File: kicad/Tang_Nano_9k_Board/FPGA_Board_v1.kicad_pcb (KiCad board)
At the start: 2 copper layers, 11 parts, among them U3 TBD62083AFG, U5 TBD62783A

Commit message: making pcb board
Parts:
- added H1: MountingHole, MountingHole:MountingHole_2.1mm, F.Cu at (103.5, 56.5)
- added H2: MountingHole, MountingHole:MountingHole_2.1mm, F.Cu at (192.4, 56.5)
- added H3: MountingHole, MountingHole:MountingHole_2.1mm, F.Cu at (192.4, 147.3)
- added H4: MountingHole, MountingHole:MountingHole_2.1mm, F.Cu at (103.5, 147.3)
- added J1: Conn_01x24, Connector_PinHeader_2.54mm:PinHeader_1x24_P2.54mm_Vertical, F.Cu at (101.6, 71.1)
- added J2: Conn_01x24, Connector_PinHeader_2.54mm:PinHeader_1x24_P2.54mm_Vertical, F.Cu at (133.3, 71.1)
- added J3: Conn_01x08, Connector_PinHeader_2.54mm:PinHeader_1x08_P2.54mm_Vertical, F.Cu at (192.4, 120.7)
- added J4: Conn_01x04, Connector_PinHeader_2.54mm:PinHeader_1x04_P2.54mm_Vertical, F.Cu at (113.7, 140.3)
- added J5: Conn_01x04, Connector_PinHeader_2.54mm:PinHeader_1x04_P2.54mm_Vertical, F.Cu at (120.2, 140.3)
- added J6: Conn_01x04, Connector_PinHeader_2.54mm:PinHeader_1x04_P2.54mm_Vertical, F.Cu at (127.0, 140.3)
- added J7: Conn_01x04, Connector_PinHeader_2.54mm:PinHeader_1x04_P2.54mm_Vertical, F.Cu at (133.3, 140.3)
- added SW1: SW_DIP_x08, Button_Switch_THT:SW_DIP_SPSTx08_Slide_9.78x22.5mm_W7.62mm_P2.54mm, F.Cu at (162.6, 139.7)
- added SW2: SW_Push, Button_Switch_SMD:Panasonic_EVQPUJ_EVQPUA, F.Cu at (180.3, 130.8)
- added SW3: SW_Push, Button_Switch_SMD:Panasonic_EVQPUJ_EVQPUA, F.Cu at (180.3, 137.4)
- added SW4: SW_Push, Button_Switch_SMD:Panasonic_EVQPUJ_EVQPUA, F.Cu at (180.3, 143.9)
- added U2: ~, BFP_footprints:OSL641501-BX, F.Cu at (177.2, 82.5)
- added U4: 74HC138, Package_DIP:CERDIP-16_W7.62mm_SideBrazed, F.Cu at (142.9, 107.3)
- R18, R19, R20, R21, R22, R23, R24, R25: value 600 -> 750; moved to B.Cu
- U1: footprint BFP:Tang_Nano_9K -> BFP_footprints:Tang_Nano_9K
- moved R22 81.4 mm to (187.3, 92.7), turned to 180 degrees
- moved R21 80.6 mm to (187.3, 86.4), turned to 180 degrees
- moved R18 80.4 mm to (187.3, 73.7), turned to 180 degrees
- moved R23 76.4 mm to (187.3, 80.0), turned to 180 degrees
- moved R19 75.3 mm to (173.4, 92.7), turned to 180 degrees
- moved R20 69.7 mm to (173.4, 86.4), turned to 180 degrees
- moved R24 61.9 mm to (173.4, 80.0), turned to 180 degrees
- moved R25 60.8 mm to (173.4, 73.7), turned to 180 degrees
- moved U5 47.2 mm to (159.4, 107.3)
- moved U1 42.5 mm to (117.5, 103.6)
- moved U3 38.8 mm to (142.9, 78.8)
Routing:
- net Net-(J2-Pin_14): track 0.00 -> 127.9 mm
- net Net-(J1-Pin_1): track 0.00 -> 125.2 mm
- net Net-(J2-Pin_13): track 0.00 -> 124.8 mm
- net Net-(J2-Pin_12): track 0.00 -> 123.6 mm
- net Net-(J1-Pin_2): track 0.00 -> 120.5 mm
- net Net-(J1-Pin_3): track 0.00 -> 116.0 mm
- net /C8: track 0.00 -> 112.2 mm
- net /C7: track 0.00 -> 109.2 mm
- net /C6: track 0.00 -> 106.1 mm
- net /C5: track 0.00 -> 103.0 mm
- net /C4: track 0.00 -> 100.0 mm
- net Net-(J2-Pin_2): track 0.00 -> 97.5 mm
- net /C3: track 0.00 -> 96.9 mm
- net /C2: track 0.00 -> 93.8 mm
- net Net-(J2-Pin_3): track 0.00 -> 92.8 mm
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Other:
- board outline added: 100 x 100 mm

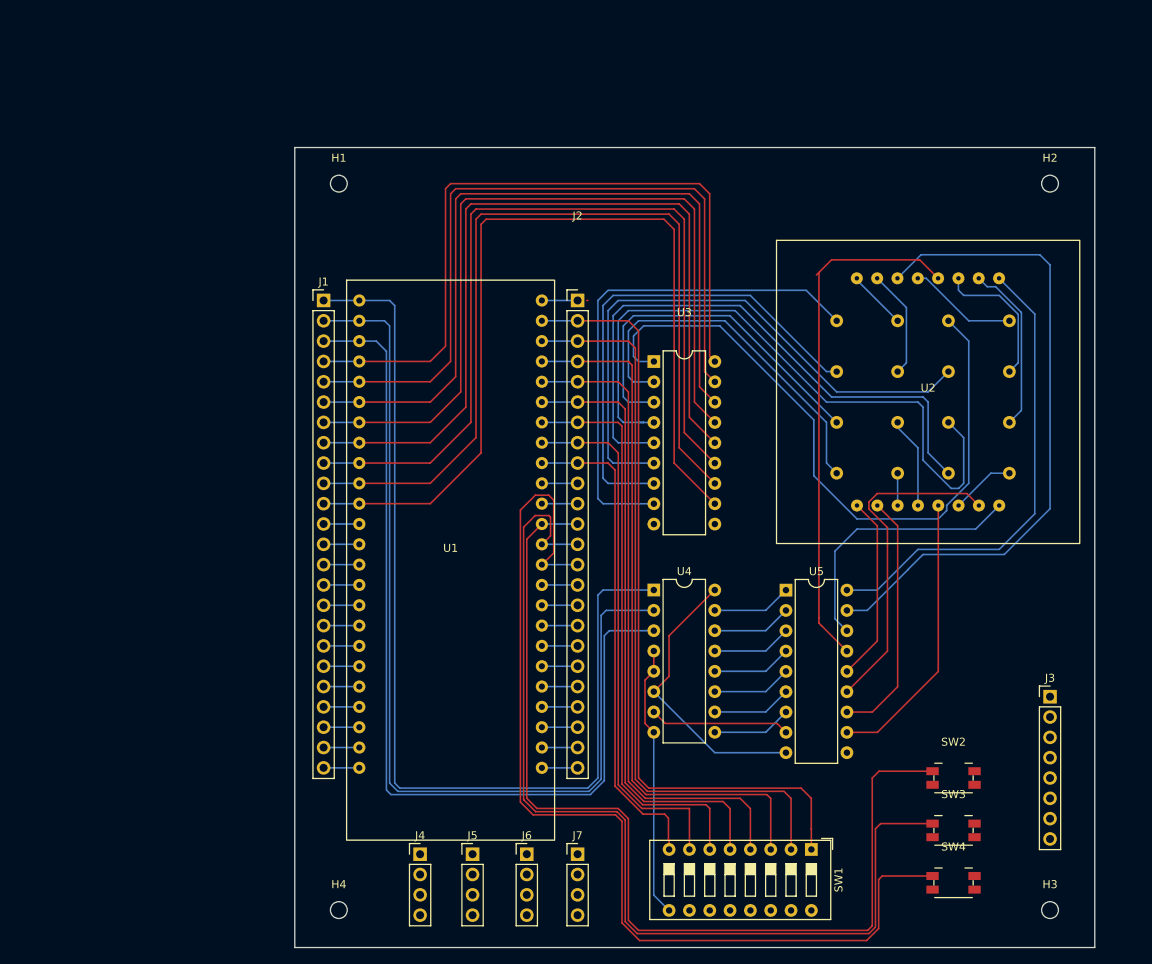
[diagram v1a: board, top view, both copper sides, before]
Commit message: set pcb position
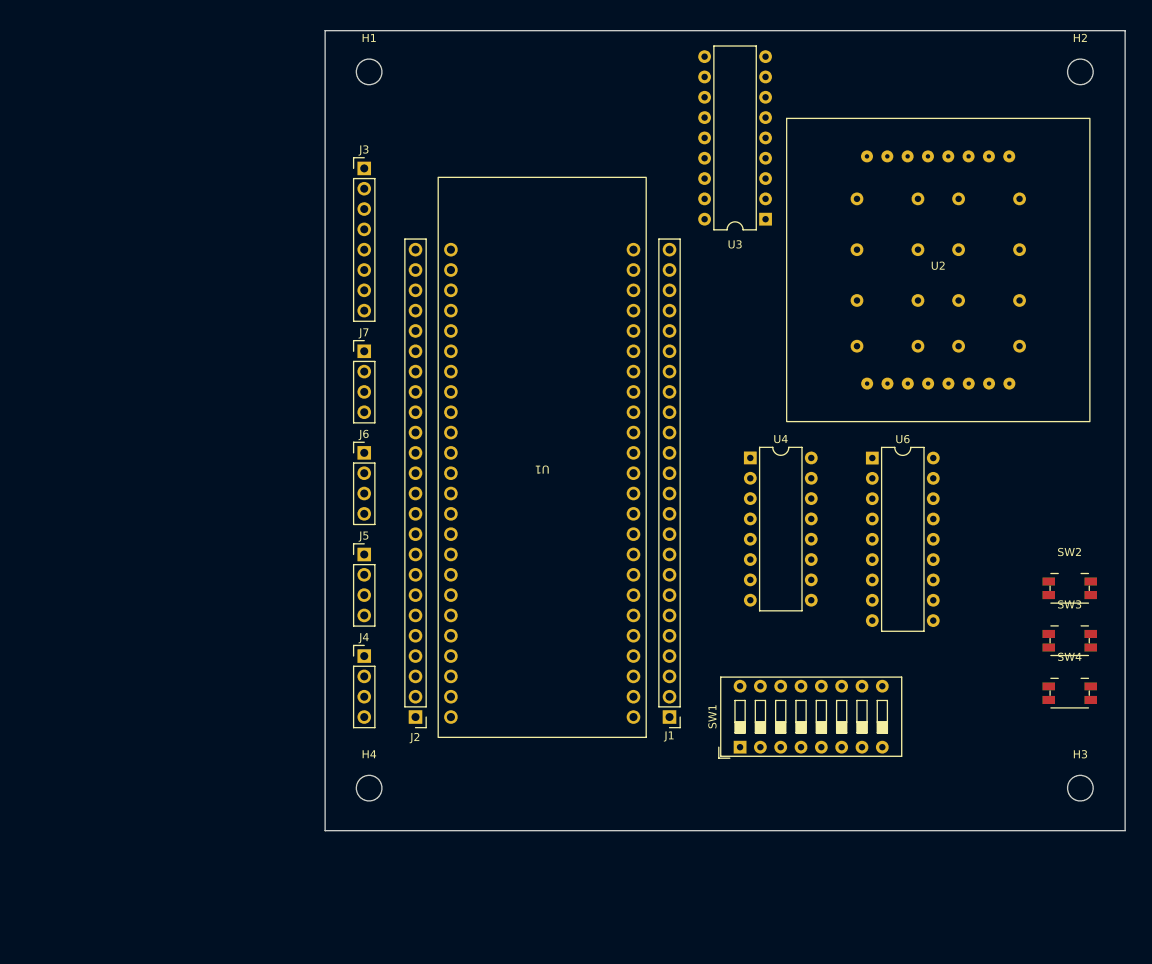
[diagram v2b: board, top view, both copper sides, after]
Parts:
- removed U5: TBD62783A, Package_DIP:DIP-18_W7.62mm
- added U6: TBD62786APG, Package_DIP:DIP-18_W7.62mm, F.Cu at (170.2, 90.8)
- H1, H2, H3, H4: footprint MountingHole:MountingHole_2.1mm -> MountingHole:MountingHole_3.2mm_M3
- moved J3 108.2 mm to (106.7, 54.6)
- moved J7 68.3 mm to (106.7, 77.5)
- moved J1 67.7 mm to (144.8, 123.2), turned to 180 degrees
- moved J2 55.9 mm to (113.1, 123.2), turned to 180 degrees
- moved J6 54.1 mm to (106.7, 90.2)
- moved J5 39.8 mm to (106.7, 102.9)
- moved SW2 27.8 mm to (194.9, 107.1)
- moved SW3 27.8 mm to (194.9, 113.7)
- moved SW4 27.8 mm to (194.9, 120.2)
- moved J4 25.7 mm to (106.7, 115.6)
- moved U3 22.6 mm to (156.8, 61.0), turned to 180 degrees
- moved U4 20.4 mm to (154.9, 90.8)
- moved U1 17.2 mm to (128.9, 90.7), turned to 180 degrees
- moved R19 16.1 mm to (175.9, 76.8)
- moved R22 15.9 mm to (188.6, 76.8)
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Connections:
- net Net-(J1-Pin_2) renamed /A1
- J1 pad 1: Net-(J1-Pin_1) -> /A2
- J1 pad 3: Net-(J1-Pin_3) -> /A0
- U1 pad 1: Net-(J1-Pin_1) -> /A2
- U1 pad 3: Net-(J1-Pin_3) -> /A0
- U4 pad 1: Net-(J1-Pin_1) -> /A0
- U4 pad 3: Net-(J1-Pin_3) -> /A2
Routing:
- net Net-(J2-Pin_14): track 127.9 -> 0.00 mm
- net Net-(J1-Pin_1): track 125.2 -> 0.00 mm
- net Net-(J2-Pin_13): track 124.8 -> 0.00 mm
- net Net-(J2-Pin_12): track 123.6 -> 0.00 mm
- net /A1: track 120.5 -> 0.00 mm
- net Net-(J1-Pin_3): track 116.0 -> 0.00 mm
- net /C8: track 112.2 -> 0.00 mm
- net /C7: track 109.2 -> 0.00 mm
- net /C6: track 106.1 -> 0.00 mm
- net /C5: track 103.0 -> 0.00 mm
- net /C4: track 100.0 -> 0.00 mm
- net Net-(J2-Pin_2): track 97.5 -> 0.00 mm
- net /C3: track 96.9 -> 0.00 mm
- net /C2: track 93.8 -> 0.00 mm
- net Net-(J2-Pin_3): track 92.8 -> 0.00 mm
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
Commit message: finish schematic, design PCB board
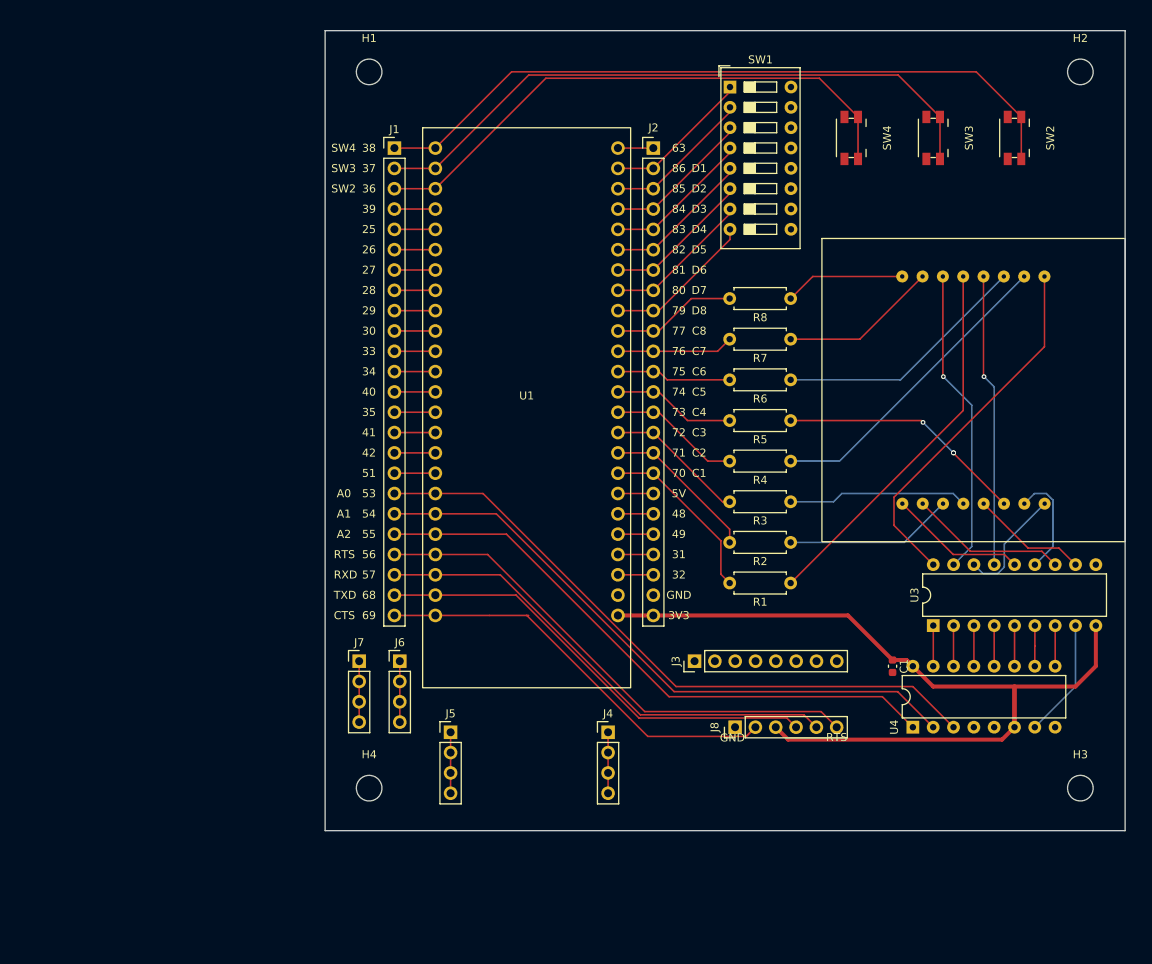
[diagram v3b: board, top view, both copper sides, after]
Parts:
- removed R18, R19, R20, R21, R22, R23, R24, R25: 750, Resistor_THT:R_Axial_DIN0207_L6.3mm_D2.5mm_P7.62mm_Horizontal
- removed U6: TBD62786APG, Package_DIP:DIP-18_W7.62mm
- added C1: 0.1μF, Capacitor_SMD:C_0603_1608Metric, F.Cu at (172.7, 116.8)
- added J8: Conn_01x06, Connector_PinHeader_2.54mm:PinHeader_1x06_P2.54mm_Vertical, F.Cu at (153.0, 124.5)
- added R1: 750, Resistor_THT:R_Axial_DIN0207_L6.3mm_D2.5mm_P7.62mm_Horizontal, F.Cu at (160.0, 106.4)
- added R2: 750, Resistor_THT:R_Axial_DIN0207_L6.3mm_D2.5mm_P7.62mm_Horizontal, F.Cu at (160.0, 101.4)
- added R3: 750, Resistor_THT:R_Axial_DIN0207_L6.3mm_D2.5mm_P7.62mm_Horizontal, F.Cu at (160.0, 96.3)
- added R4: 750, Resistor_THT:R_Axial_DIN0207_L6.3mm_D2.5mm_P7.62mm_Horizontal, F.Cu at (160.0, 91.2)
- added R5: 750, Resistor_THT:R_Axial_DIN0207_L6.3mm_D2.5mm_P7.62mm_Horizontal, F.Cu at (160.0, 86.1)
- added R6: 750, Resistor_THT:R_Axial_DIN0207_L6.3mm_D2.5mm_P7.62mm_Horizontal, F.Cu at (160.0, 81.0)
- added R7: 750, Resistor_THT:R_Axial_DIN0207_L6.3mm_D2.5mm_P7.62mm_Horizontal, F.Cu at (160.0, 76.0)
- added R8: 750, Resistor_THT:R_Axial_DIN0207_L6.3mm_D2.5mm_P7.62mm_Horizontal, F.Cu at (160.0, 70.9)
- U3: value TBD62083AFG -> TBD62786APG
- moved SW1 82.5 mm to (152.4, 44.4), turned to 0 degrees
- moved J1 79.0 mm to (110.5, 52.1), turned to 0 degrees
- moved J2 77.1 mm to (142.8, 52.1), turned to 0 degrees
- moved SW4 74.6 mm to (167.6, 50.8), turned to -90 degrees
- moved J3 74.2 mm to (148.0, 116.2), turned to 90 degrees
- moved SW3 65.1 mm to (177.8, 50.8), turned to -90 degrees
- moved SW2 56.7 mm to (188.0, 50.8), turned to -90 degrees
- moved U3 55.0 mm to (177.8, 111.8), turned to 90 degrees
- moved U4 39.3 mm to (175.3, 124.5), turned to 90 degrees
- moved J7 38.7 mm to (106.0, 116.2)
- moved J4 31.9 mm to (137.2, 125.1)
- moved J6 26.4 mm to (111.1, 116.2)
- moved J5 24.7 mm to (117.5, 125.1)
- moved U2 15.6 mm to (182.8, 82.3)
- moved U1 6.50 mm to (127.0, 84.5), turned to 0 degrees
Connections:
- net Net-(J1-Pin_21) renamed /RTS
- net Net-(J1-Pin_22) renamed /RXD
- net Net-(J1-Pin_23) renamed /TXD
- net Net-(J1-Pin_24) renamed /CTS
- J1 pad 1: /A2 -> Net-(J1-Pin_1)
- J1 pad 10: /C7 -> Net-(J1-Pin_10)
- J1 pad 11: /C8 -> Net-(J1-Pin_11)
- J1 pad 18: Net-(J1-Pin_18) -> /A2
- J1 pad 19: Net-(J1-Pin_19) -> /A1
- J1 pad 2: /A1 -> Net-(J1-Pin_2)
- J1 pad 20: Net-(J1-Pin_20) -> /A0
- J1 pad 3: /A0 -> Net-(J1-Pin_3)
- J1 pad 4: /C1 -> Net-(J1-Pin_4)
- J1 pad 5: /C2 -> Net-(J1-Pin_5)
- J1 pad 6: /C3 -> Net-(J1-Pin_6)
- J1 pad 7: /C4 -> Net-(J1-Pin_7)
- J1 pad 8: /C5 -> Net-(J1-Pin_8)
- J1 pad 9: /C6 -> Net-(J1-Pin_9)
- J2 pad 10: Net-(J2-Pin_10) -> /C8
- J2 pad 11: Net-(J2-Pin_11) -> /C7
- J2 pad 12: Net-(J2-Pin_12) -> /C6
- J2 pad 13: Net-(J2-Pin_13) -> /C5
- J2 pad 14: Net-(J2-Pin_14) -> /C4
- J2 pad 15: Net-(J2-Pin_15) -> /C3
- J2 pad 16: Net-(J2-Pin_16) -> /C2
- J2 pad 17: Net-(J2-Pin_17) -> /C1
- SW2 pad 1: Net-(J2-Pin_12) -> Net-(J1-Pin_1)
- SW3 pad 1: Net-(J2-Pin_13) -> Net-(J1-Pin_2)
- SW4 pad 1: Net-(J2-Pin_14) -> Net-(J1-Pin_3)
- U1 pad 1: /A2 -> Net-(J1-Pin_1)
- U1 pad 10: /C7 -> Net-(J1-Pin_10)
- U1 pad 11: /C8 -> Net-(J1-Pin_11)
- U1 pad 18: Net-(J1-Pin_18) -> /A2
- U1 pad 19: Net-(J1-Pin_19) -> /A1
- U1 pad 2: /A1 -> Net-(J1-Pin_2)
- U1 pad 20: Net-(J1-Pin_20) -> /A0
- U1 pad 3: /A0 -> Net-(J1-Pin_3)
- U1 pad 32: Net-(J2-Pin_17) -> /C1
- U1 pad 33: Net-(J2-Pin_16) -> /C2
- U1 pad 34: Net-(J2-Pin_15) -> /C3
- U1 pad 35: Net-(J2-Pin_14) -> /C4
- U1 pad 36: Net-(J2-Pin_13) -> /C5
- U1 pad 37: Net-(J2-Pin_12) -> /C6
- U1 pad 38: Net-(J2-Pin_11) -> /C7
- U1 pad 39: Net-(J2-Pin_10) -> /C8
- U1 pad 4: /C1 -> Net-(J1-Pin_4)
- U1 pad 5: /C2 -> Net-(J1-Pin_5)
- U1 pad 6: /C3 -> Net-(J1-Pin_6)
- U1 pad 7: /C4 -> Net-(J1-Pin_7)
- U1 pad 8: /C5 -> Net-(J1-Pin_8)
- U1 pad 9: /C6 -> Net-(J1-Pin_9)
- U3 pad 11: /C8 -> Net-(U2-R8)
- U3 pad 12: /C7 -> Net-(U2-R7)
- U3 pad 13: /C6 -> Net-(U2-R6)
- U3 pad 14: /C5 -> Net-(U2-R5)
- U3 pad 15: /C4 -> Net-(U2-R4)
- U3 pad 16: /C3 -> Net-(U2-R3)
- U3 pad 17: /C2 -> Net-(U2-R2)
- U3 pad 18: /C1 -> Net-(U2-R1)
- U3 pad 9: unconnected-(U3-COMMON-Pad9) -> +3V3
- U4 pad 10: Net-(U4-~{Y5}) -> Net-(U3-I6)
- U4 pad 11: Net-(U4-~{Y4}) -> Net-(U3-I5)
- U4 pad 12: Net-(U4-~{Y3}) -> Net-(U3-I4)
- U4 pad 13: Net-(U4-~{Y2}) -> Net-(U3-I3)
- U4 pad 14: Net-(U4-~{Y1}) -> Net-(U3-I2)
- U4 pad 15: Net-(U4-~{Y0}) -> Net-(U3-I1)
- U4 pad 7: Net-(U4-~{Y7}) -> Net-(U3-I8)
- U4 pad 9: Net-(U4-~{Y6}) -> Net-(U3-I7)
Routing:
- net +3V3: track 0.00 -> 105.8 mm
- net Net-(J1-Pin_1): track 0.00 -> 89.9 mm
- net /A2: track 0.00 -> 82.0 mm
- net Net-(J1-Pin_2): track 0.00 -> 80.5 mm
- net /A1: track 0.00 -> 78.4 mm
- net /A0: track 0.00 -> 74.8 mm
- net Net-(J1-Pin_3): track 0.00 -> 70.9 mm
- net /RTS: track 0.00 -> 64.2 mm
- net /RXD: track 0.00 -> 60.6 mm
- net /TXD: track 0.00 -> 57.0 mm
- net /CTS: track 0.00 -> 53.9 mm
- net Net-(U2-C1): track 0.00 -> 47.3 mm
- net Net-(U2-R1): track 0.00 -> 45.8 mm
- net Net-(U2-C4): track 0.00 -> 38.8 mm
- net Net-(U2-R2): track 0.00 -> 38.5 mm, vias 0 -> 1
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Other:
- board text added: "25"
- board text added: "26"
- board text added: "27"
- board text added: "28"
- board text added: "29"
- board text added: "30"
- board text added: "31"
- board text added: "32"
- board text added: "33"
- board text added: "34"
- board text added: "35"
- board text added: "36"
- board text added: "37"
- board text added: "38"
- board text added: "39"
- board text added: "3V3"
- board text added: "40"
- board text added: "41"
- board text added: "42"
- board text added: "48"
- board text added: "49"
- board text added: "51"
- board text added: "53"
- board text added: "54"
- board text added: "55"
- board text added: "56"
- board text added: "57"
- board text added: "5V"
- board text added: "63"
- board text added: "68"
- board text added: "69"
- board text added: "70"
- board text added: "71"
- board text added: "72"
- board text added: "73"
- board text added: "74"
- board text added: "75"
- board text added: "76"
- board text added: "77"
- board text added: "79"
- board text added: "80"
- board text added: "81"
- board text added: "82"
- board text added: "83"
- board text added: "84"
- board text added: "85"
- board text added: "86"
- board text added: "A0"
- board text added: "A1"
- board text added: "A2"
- board text added: "C1"
- board text added: "C2"
- board text added: "C3"
- board text added: "C4"
- board text added: "C5"
- board text added: "C6"
- board text added: "C7"
- board text added: "C8"
- board text added: "CTS"
- board text added: "D1"
- board text added: "D2"
- board text added: "D3"
- board text added: "D4"
- board text added: "D5"
- board text added: "D6"
- board text added: "D7"
- board text added: "D8"
- board text added: "GND"
- board text added: "RTS"
- board text added: "RXD"
- board text added: "SW2"
- board text added: "SW3"
- board text added: "SW4"
- board text added: "TXD"

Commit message: Reviewed PCB board
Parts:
- moved U2 0.55 mm to (182.3, 82.3)
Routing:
- net Net-(U2-C5): track 31.0 -> 75.2 mm, vias 3 -> 0
- net Net-(U2-C1): track 47.3 -> 70.8 mm
- net Net-(U2-C4): track 38.8 -> 61.5 mm
- net Net-(U2-R1): track 45.8 -> 64.9 mm
- net Net-(U2-R4): track 36.6 -> 54.9 mm, vias 1 -> 0
- net Net-(U2-R3): track 14.6 -> 30.6 mm
- net Net-(U2-C6): track 32.0 -> 47.0 mm
- net Net-(U3-I8): track 14.8 -> 22.9 mm
- net Net-(U2-R6): track 13.5 -> 8.39 mm
- net Net-(U2-R7): track 19.7 -> 21.7 mm
- net Net-(J1-Pin_3): track 70.9 -> 72.0 mm
- net Net-(J1-Pin_2): track 80.5 -> 81.5 mm
- net Net-(J1-Pin_1): track 89.9 -> 90.9 mm
- net Net-(U2-C8): track 15.1 -> 14.5 mm
- net Net-(U2-C2): track 21.1 -> 20.5 mm
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- added copper zone on B.Cu, net GND
- added copper zone on F.Cu, net GND
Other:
- board text added: "Tang Nano 9K Board Made by BFP Team"
- board text added: "VCC"
